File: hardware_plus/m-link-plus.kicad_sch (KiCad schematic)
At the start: 31 parts, among them J3 SIG, J4 PROGRAM, J5 I2C, SW1 RESTORE SETTINGS, U1 AP1117-33, U2 DRV8837C, U3 DRV8837C, U4 ESP-12F, U5 PCA9685PW, U6 DRV8837C

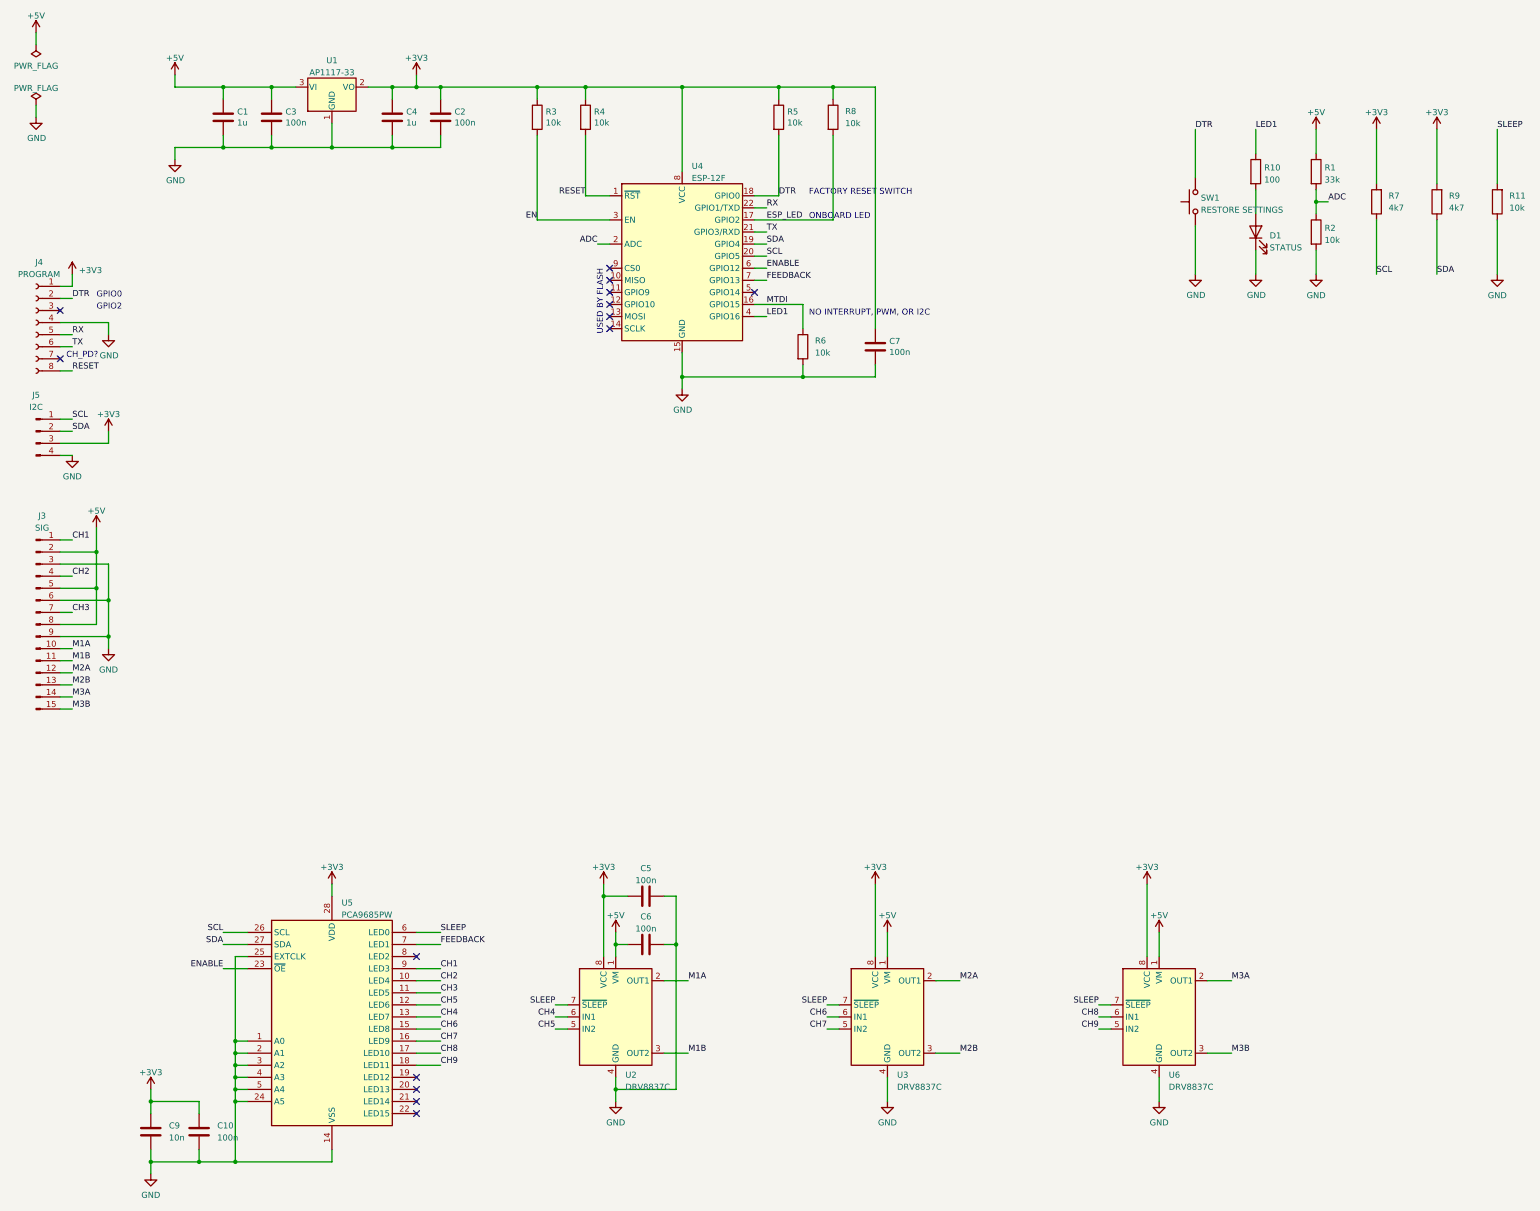
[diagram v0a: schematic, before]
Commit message: Remove unnecessary resistors and begin improving layout.
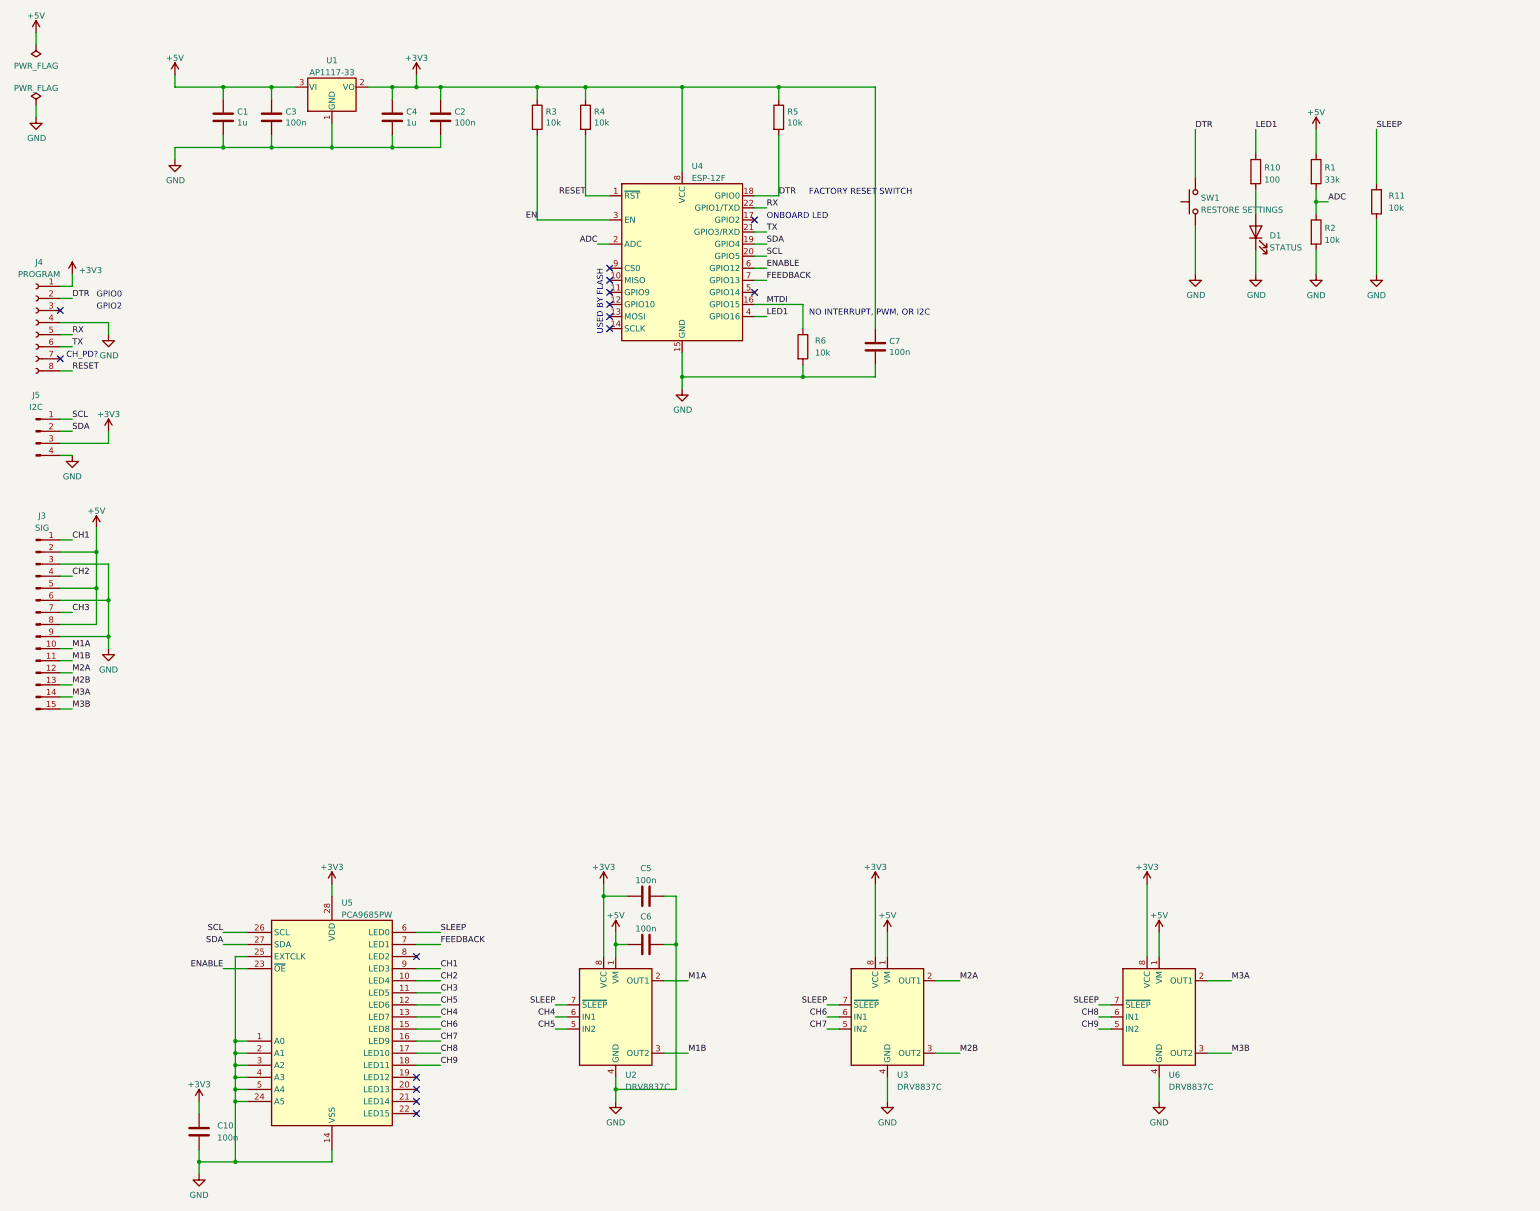
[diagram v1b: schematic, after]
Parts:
- removed C9: 10n, Capacitor_SMD:C_0603_1608Metric, symbol Device:C
- removed R7, R9: 4k7, Resistor_SMD:R_0603_1608Metric, symbol Device:R
- removed R8: 10k, Resistor_SMD:R_0603_1608Metric, symbol Device:R
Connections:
- net ESP_LED: no longer names the net of U4.17 (GPIO2)
- no-connect marks 14 -> 15
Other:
- moved on the sheet: R11
